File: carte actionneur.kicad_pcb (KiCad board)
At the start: 2 copper layers, 47 parts, among them J1 Conn_01x03_Pin, J10 Conn_01x03_Pin, J11 Conn_01x02, J12 Screw_Terminal_01x02, J13 Screw_Terminal_01x02, J14 Screw_Terminal_01x02, J15 Conn_01x02, J2 Conn_01x02, J3 Conn_01x03_Pin, J4 Conn_01x03_Pin, J5 Connecteur Programmation, J6 Conn_01x03_Pin, J7 Conn_01x03_Pin, J8 Conn_01x03_Pin, J9 Conn_01x03_Pin, Q1 BSS83P, Q2 2N7000, U1 MEGA_PRO_EMBED_CH340G___ATMEG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, U2 LM317_TO-252, U3 ZXBM5210-SP, U4 YAAJ_DCDC_StepDown_LM2596, U5 YAAJ_DCDC_StepDown_LM2596, U6 YAAJ_DCDC_StepDown_LM2596, U7 ZXBM5210-SP

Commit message: test git
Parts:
- added J16: Screw_Terminal_01x02, TerminalBlockBend:CUI_TBP01R1-508-02BE, F.Cu at (77.0, 130.6)
- added J17: Screw_Terminal_01x04, TerminalBlockBend:CUI_TBP01R1-508-04BE, F.Cu at (95.8, 120.4)
- added J18: Conn_01x04_Pin, Connector:FanPinHeader_1x04_P2.54mm_Vertical, F.Cu at (94.0, 127.8)
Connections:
- A1 pad 3: unconnected-(A1-1B-Pad3) -> Net-(A1-1B)
- A1 pad 4: unconnected-(A1-1A-Pad4) -> Net-(A1-1A)
- A1 pad 5: unconnected-(A1-2A-Pad5) -> Net-(A1-2A)
- A1 pad 6: unconnected-(A1-2B-Pad6) -> Net-(A1-2B)

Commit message: shema complet
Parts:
- removed C1: 0.1uF, Capacitor_SMD:C_0805_2012Metric
- removed C2: 1uF, Capacitor_SMD:C_0805_2012Metric
- removed H5, H6, H7, H8: MountingHole_Pad, MountingHole:MountingHole_2.7mm_Pad_Via
- removed J12, J13, J14, J16: Screw_Terminal_01x02, TerminalBlockBend:CUI_TBP01R1-508-02BE
- removed J18: Conn_01x04_Pin, Connector:FanPinHeader_1x04_P2.54mm_Vertical
- removed J4: Conn_01x03_Pin, Connector_PinHeader_2.54mm:PinHeader_1x03_P2.54mm_Vertical
- removed R2: 4.7k, Resistor_SMD:R_0805_2012Metric
- removed R3: 1.5k, Resistor_SMD:R_0805_2012Metric
- removed U6: YAAJ_DCDC_StepDown_LM2596, lib-buck-converter:YAAJ_DCDC_StepDown_LM2596
- added A2: Pololu_Breakout_A4988, Module:Pololu_Breakout-16_15.2x20.3mm, F.Cu at (222.9, 94.2)
- added A3: Pololu_Breakout_A4988, Module:Pololu_Breakout-16_15.2x20.3mm, F.Cu at (239.7, 94.2)
- added C7: 100µ, Capacitor_THT:CP_Radial_D8.0mm_P3.50mm, F.Cu at (224.1, 118.8)
- added C8: 100µ, Capacitor_THT:CP_Radial_D8.0mm_P3.50mm, F.Cu at (224.1, 128.3)
- added C9: 100µ, Capacitor_THT:CP_Radial_D8.0mm_P3.50mm, F.Cu at (224.1, 137.9)
- added D3: D, Diode_SMD:D_SOD-123, F.Cu at (265.0, 133.1)
- added D4: D, Diode_SMD:D_SOD-123, F.Cu at (265.0, 136.4)
- added D5: D, Diode_SMD:D_SOD-123, F.Cu at (265.0, 139.8)
- added J19: Conn_01x04_Pin, Connector_JST:JST_XH_B4B-XH-A_1x04_P2.50mm_Vertical, F.Cu at (257.9, 95.5)
- added J21: Conn_01x08_Pin, Connector_PinHeader_2.54mm:PinHeader_1x08_P2.54mm_Vertical, F.Cu at (259.8, 116.3)
- added J22: Conn_01x02_Pin, Connector_JST:JST_XH_B2B-XH-A_1x02_P2.50mm_Vertical, F.Cu at (251.5, 117.4)
- added J23: Conn_01x02_Pin, Connector_JST:JST_XH_B2B-XH-A_1x02_P2.50mm_Vertical, F.Cu at (251.5, 125.2)
- added J24: Conn_01x02_Pin, Connector_JST:JST_XH_B2B-XH-A_1x02_P2.50mm_Vertical, F.Cu at (251.5, 133.0)
- added J25: Conn_01x03_Pin, Connector_PinHeader_2.54mm:PinHeader_1x03_P2.54mm_Vertical, F.Cu at (256.8, 102.3)
- added J26: Conn_01x03_Pin, Connector_PinHeader_2.54mm:PinHeader_1x03_P2.54mm_Vertical, F.Cu at (261.4, 102.3)
- added J27: Conn_01x03_Pin, Connector_PinHeader_2.54mm:PinHeader_1x03_P2.54mm_Vertical, F.Cu at (266.1, 102.3)
- added JP1: Jumper_2_Open, Jumper:SolderJumper-2_P1.3mm_Open_TrianglePad1.0x1.5mm, F.Cu at (232.8, 115.8)
- added JP10: Jumper_2_Open, Jumper:SolderJumper-2_P1.3mm_Open_TrianglePad1.0x1.5mm, F.Cu at (237.1, 122.9)
- added JP11: Jumper_2_Open, Jumper:SolderJumper-2_P1.3mm_Open_TrianglePad1.0x1.5mm, F.Cu at (237.1, 126.4)
- added JP12: Jumper_2_Open, Jumper:SolderJumper-2_P1.3mm_Open_TrianglePad1.0x1.5mm, F.Cu at (237.1, 130.0)
- added JP13: Jumper_2_Open, Jumper:SolderJumper-2_P1.3mm_Open_TrianglePad1.0x1.5mm, F.Cu at (237.1, 133.5)
- added JP14: Jumper_2_Open, Jumper:SolderJumper-2_P1.3mm_Open_TrianglePad1.0x1.5mm, F.Cu at (237.1, 137.1)
- added JP15: Jumper_2_Open, Jumper:SolderJumper-2_P1.3mm_Open_TrianglePad1.0x1.5mm, F.Cu at (241.5, 115.8)
- added JP16: Jumper_2_Open, Jumper:SolderJumper-2_P1.3mm_Open_TrianglePad1.0x1.5mm, F.Cu at (241.5, 119.3)
- added JP17: Jumper_2_Open, Jumper:SolderJumper-2_P1.3mm_Open_TrianglePad1.0x1.5mm, F.Cu at (241.5, 122.9)
- added JP18: Jumper_2_Open, Jumper:SolderJumper-2_P1.3mm_Open_TrianglePad1.0x1.5mm, F.Cu at (241.5, 126.4)
- added JP19: Jumper_2_Open, Jumper:SolderJumper-2_P1.3mm_Open_TrianglePad1.0x1.5mm, F.Cu at (241.5, 130.0)
- added JP2: Jumper_2_Open, Jumper:SolderJumper-2_P1.3mm_Open_TrianglePad1.0x1.5mm, F.Cu at (232.8, 119.3)
- added JP20: Jumper_2_Open, Jumper:SolderJumper-2_P1.3mm_Open_TrianglePad1.0x1.5mm, F.Cu at (241.5, 133.5)
- added JP21: Jumper_2_Open, Jumper:SolderJumper-2_P1.3mm_Open_TrianglePad1.0x1.5mm, F.Cu at (241.5, 137.1)
- added JP22: Jumper_2_Open, Jumper:SolderJumper-2_P1.3mm_Open_TrianglePad1.0x1.5mm, F.Cu at (245.8, 115.8)
- added JP23: Jumper_2_Open, Jumper:SolderJumper-2_P1.3mm_Open_TrianglePad1.0x1.5mm, F.Cu at (245.8, 119.3)
- added JP24: Jumper_2_Open, Jumper:SolderJumper-2_P1.3mm_Open_TrianglePad1.0x1.5mm, F.Cu at (245.8, 122.9)
- added JP3: Jumper_2_Open, Jumper:SolderJumper-2_P1.3mm_Open_TrianglePad1.0x1.5mm, F.Cu at (232.8, 122.9)
- added JP4: Jumper_2_Open, Jumper:SolderJumper-2_P1.3mm_Open_TrianglePad1.0x1.5mm, F.Cu at (232.8, 126.4)
- added JP5: Jumper_2_Open, Jumper:SolderJumper-2_P1.3mm_Open_TrianglePad1.0x1.5mm, F.Cu at (232.8, 130.0)
- added JP6: Jumper_2_Open, Jumper:SolderJumper-2_P1.3mm_Open_TrianglePad1.0x1.5mm, F.Cu at (232.8, 133.5)
- added JP7: Jumper_2_Open, Jumper:SolderJumper-2_P1.3mm_Open_TrianglePad1.0x1.5mm, F.Cu at (232.8, 137.1)
- added JP8: Jumper_2_Open, Jumper:SolderJumper-2_P1.3mm_Open_TrianglePad1.0x1.5mm, F.Cu at (237.1, 115.8)
- added JP9: Jumper_2_Open, Jumper:SolderJumper-2_P1.3mm_Open_TrianglePad1.0x1.5mm, F.Cu at (237.1, 119.3)
- added Q3: QM6006D, Package_TO_SOT_SMD:TO-252-2, F.Cu at (166.3, 147.2)
- added Q4: QM6006D, Package_TO_SOT_SMD:TO-252-2, F.Cu at (168.5, 133.0)
- added R10: 100k, Resistor_SMD:R_0805_2012Metric, F.Cu at (270.1, 135.8)
- added R11: 100k, Resistor_SMD:R_0805_2012Metric, F.Cu at (270.1, 138.8)
- added R9: 100k, Resistor_SMD:R_0805_2012Metric, F.Cu at (270.1, 132.8)
- J17: value Screw_Terminal_01x04 -> Conn_01x04_Pin; footprint TerminalBlockBend:CUI_TBP01R1-508-04BE -> Connector_JST:JST_XH_B4B-XH-A_1x04_P2.50mm_Vertical
- J2: footprint TerminalBlock:TerminalBlock_bornier-2_P5.08mm -> TerminalBlockBend:CUI_TBP01R1-508-02BE
- J3: value Conn_01x03_Pin -> Conn_01x04_Pin; footprint Connector_PinHeader_2.54mm:PinHeader_1x03_P2.54mm_Vertical -> Connector_JST:JST_XH_B4B-XH-A_1x04_P2.50mm_Vertical
- J6: value Conn_01x03_Pin -> Conn_01x08_Pin; footprint Connector_PinHeader_2.54mm:PinHeader_1x03_P2.54mm_Vertical -> Connector_PinHeader_2.54mm:PinHeader_1x08_P2.54mm_Vertical
- Q1: value BSS83P -> Q_NMOS_GDS; footprint Package_TO_SOT_SMD:SOT-23 -> Package_TO_SOT_SMD:TO-252-2
- Q2: value 2N7000 -> QM6006D; footprint Package_TO_SOT_THT:TO-92_Inline -> Package_TO_SOT_SMD:TO-252-2
- R1: value 10k -> 56k; footprint Resistor_SMD:R_0805_2012Metric -> Resistor_SMD:R_0805_2012Metric_Pad1.20x1.40mm_HandSolder
- U2: value LM317_TO-252 -> YAAJ_DCDC_StepDown_LM2596; footprint Package_TO_SOT_SMD:TO-252-2 -> lib-buck-converter:YAAJ_DCDC_StepDown_LM2596
- moved Q2 99.4 mm to (169.8, 118.7)
- moved U2 50.0 mm to (189.2, 17.1)
- moved J2 11.2 mm to (152.2, 31.5)
- moved J3 9.07 mm to (190.2, 63.5)
- moved Q1 8.89 mm to (175.8, 47.5)
- moved J6 3.61 mm to (205.0, 64.7)
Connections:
- A1 pad 1: unconnected-(A1-GND-Pad1) -> GND
- A1 pad 10: unconnected-(A1-MS1-Pad10) -> Net-(A1-MS1)
- A1 pad 11: unconnected-(A1-MS2-Pad11) -> Net-(A1-MS2)
- A1 pad 12: unconnected-(A1-MS3-Pad12) -> Net-(A1-MS3)
- A1 pad 13: unconnected-(A1-~{RESET}-Pad13) -> Reset
- A1 pad 14: unconnected-(A1-~{SLEEP}-Pad14) -> Sleep
- A1 pad 15: unconnected-(A1-STEP-Pad15) -> STEP1
- A1 pad 16: unconnected-(A1-DIR-Pad16) -> DIR1
- A1 pad 2: unconnected-(A1-VDD-Pad2) -> +5V
- A1 pad 7: unconnected-(A1-GND-Pad7) -> GND
- A1 pad 8: unconnected-(A1-VMOT-Pad8) -> 12V Mot
- A1 pad 9: unconnected-(A1-~{ENABLE}-Pad9) -> Enable3
- C3 pad 1: tension alim moteur DC -> +5V
- C4 pad 1: +12V -> Net-(JP19-A)
- C5 pad 1: tension alim moteur DC -> +5V
- C6 pad 1: +12V -> Net-(JP22-A)
- D1 pad 1: +12V -> Net-(D1-K)
- D1 pad 2: Net-(D1-A) -> GND
- J1 pad 1: GND -> Servo4
- J1 pad 2: 5V -> 5VServo
- J1 pad 3: Net-(J1-Pin_3) -> GND
- J10 pad 1: Net-(J10-Pin_1) -> Servo3
- J10 pad 2: 5V -> 5VServo
- J17 pad 1: Net-(A1-1B) -> Net-(A2-2B)
- J17 pad 2: Net-(A1-1A) -> Net-(A2-2A)
- J17 pad 3: Net-(A1-2A) -> Net-(A2-1A)
- J17 pad 4: Net-(A1-2B) -> Net-(A2-1B)
- J2 pad 1: GND -> Net-(J2-Pin_1)
- J2 pad 2: Net-(J2-Pin_2) -> +24V
- J3 pad 1: GND -> Net-(A3-2B)
- J3 pad 2: 5V -> Net-(A3-2A)
- J3 pad 3: Net-(J3-Pin_3) -> Net-(A3-1A)
- J6 pad 1: GND -> Net-(J6-Pin_1)
- J6 pad 2: 5V -> Net-(J6-Pin_2)
- J7 pad 1: Net-(J7-Pin_1) -> Servo1
- J7 pad 2: 5V -> 5VServo
- J8 pad 1: Net-(J8-Pin_1) -> Servo2
- J8 pad 2: 5V -> 5VServo
- J9 pad 1: Net-(J9-Pin_1) -> Servo8
- J9 pad 2: 5V -> 5VServo
- Q1 pad 1: Net-(D1-A) -> Net-(D1-K)
- Q1 pad 2: +12V -> Net-(J2-Pin_1)
- Q1 pad 3: Net-(J2-Pin_2) -> GND
- Q2 pad 1: unconnected-(Q2-S-Pad1) -> ctrlActionneur1
- Q2 pad 2: unconnected-(Q2-G-Pad2) -> Net-(D3-A)
- Q2 pad 3: unconnected-(Q2-D-Pad3) -> GND
- R1 pad 1: Net-(D1-A) -> +24V
- R1 pad 2: GND -> Net-(D1-K)
- U1 pad A0: unconnected-(U1-PadA0) -> Net-(J21-Pin_8)
- U1 pad A1: unconnected-(U1-PadA1) -> Net-(J6-Pin_1)
- U1 pad A10: unconnected-(U1-PadA10) -> Net-(J21-Pin_3)
- U1 pad A11: unconnected-(U1-PadA11) -> Net-(J6-Pin_6)
- U1 pad A12: unconnected-(U1-PadA12) -> Net-(J21-Pin_2)
- U1 pad A13: unconnected-(U1-PadA13) -> Net-(J6-Pin_7)
- U1 pad A14: unconnected-(U1-PadA14) -> Net-(J21-Pin_1)
- U1 pad A15: unconnected-(U1-PadA15) -> Net-(J6-Pin_8)
- U1 pad A2: unconnected-(U1-PadA2) -> Net-(J21-Pin_7)
- U1 pad A3: unconnected-(U1-PadA3) -> Net-(J6-Pin_2)
- U1 pad A4: unconnected-(U1-PadA4) -> Net-(J21-Pin_6)
- U1 pad A5: unconnected-(U1-PadA5) -> Net-(J6-Pin_3)
- U1 pad A6: unconnected-(U1-PadA6) -> Net-(J21-Pin_5)
- U1 pad A7: unconnected-(U1-PadA7) -> Net-(J6-Pin_4)
- U1 pad A8: unconnected-(U1-PadA8) -> Net-(J21-Pin_4)
- U1 pad A9: unconnected-(U1-PadA9) -> Net-(J6-Pin_5)
- U1 pad D10: FWD1 -> Servo6
- U1 pad D11: REV1 -> Servo5
- U1 pad D12: FWD2 -> Servo8
- U1 pad D13: REV2 -> Servo7
- U1 pad D2: Net-(J7-Pin_1) -> STEP2
- U1 pad D20: unconnected-(U1-PadD20) -> SWDIO
- U1 pad D21: unconnected-(U1-PadD21) -> SWCLK
- U1 pad D22: unconnected-(U1-PadD22) -> Sleep
- U1 pad D23: unconnected-(U1-PadD23) -> Reset
- U1 pad D24: unconnected-(U1-PadD24) -> Enable3
- U1 pad D25: unconnected-(U1-PadD25) -> DIR1
- U1 pad D26: unconnected-(U1-PadD26) -> Enable2
- U1 pad D27: unconnected-(U1-PadD27) -> DIR2
- U1 pad D28: unconnected-(U1-PadD28) -> Enable1
- U1 pad D29: unconnected-(U1-PadD29) -> DIR3
- U1 pad D3: Net-(J1-Pin_3) -> STEP1
- U1 pad D4: Net-(J8-Pin_1) -> ctrlActionneur1
- U1 pad D42: unconnected-(U1-PadD42) -> ctrlActionneur2
- U1 pad D43: unconnected-(U1-PadD43) -> ctrlActionneur3
- U1 pad D44: unconnected-(U1-PadD44) -> REV2
- U1 pad D45: unconnected-(U1-PadD45) -> REV1
- U1 pad D46: unconnected-(U1-PadD46) -> FWD1
- U1 pad D5: Net-(J3-Pin_3) -> STEP3
- U1 pad D52: unconnected-(U1-PadD52) -> FWD2
- U1 pad D6: Net-(J9-Pin_1) -> Servo2
- U1 pad D7: Net-(J4-Pin_3) -> Servo1
- U1 pad D8: Net-(J10-Pin_1) -> Servo4
- U1 pad D9: Net-(J6-Pin_3) -> Servo3
- U1 pad VIN_1: +12V -> 12V Mot
- U1 pad VIN_2: +12V -> 12V Mot
- U2 pad 1: Net-(U2-ADJ) -> +24V
- U2 pad 2: +5V -> GND
- U2 pad 3: +12V -> GND
- U3 pad 2: +12V -> Net-(JP19-A)
- U3 pad 3: tension alim moteur DC -> +5V
- U3 pad 6: tension alim moteur DC -> +5V
- U4 pad 1: Net-(J12-Pin_1) -> +24V
- U4 pad 4: tension alim moteur DC -> VmotDC
- U5 pad 1: Net-(J13-Pin_1) -> +24V
- U5 pad 4: 5V -> 12V Mot
- U7 pad 2: +12V -> Net-(JP22-A)
- U7 pad 3: tension alim moteur DC -> +5V
- U7 pad 6: tension alim moteur DC -> +5V

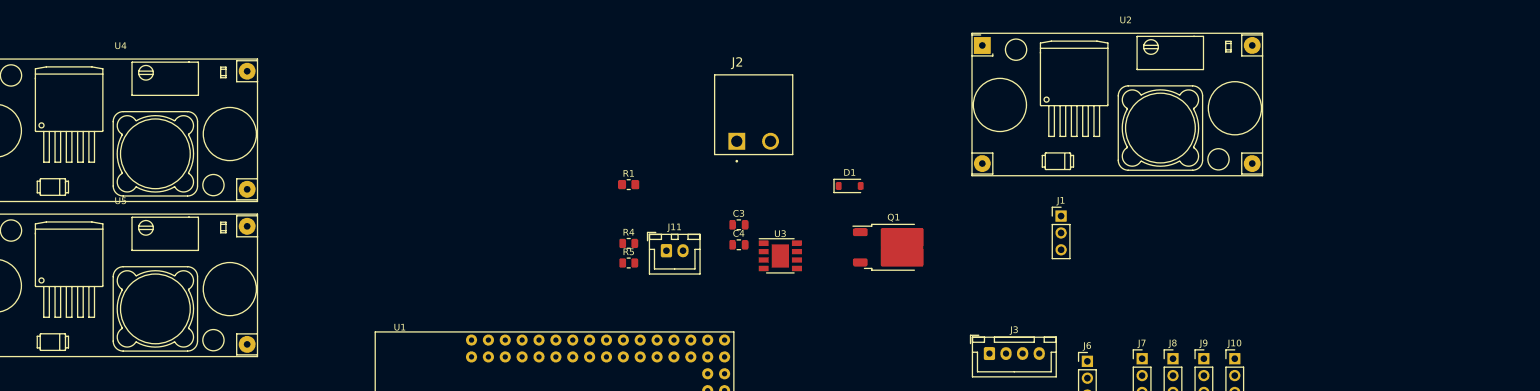
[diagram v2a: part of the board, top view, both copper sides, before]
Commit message: ajout prise capteur
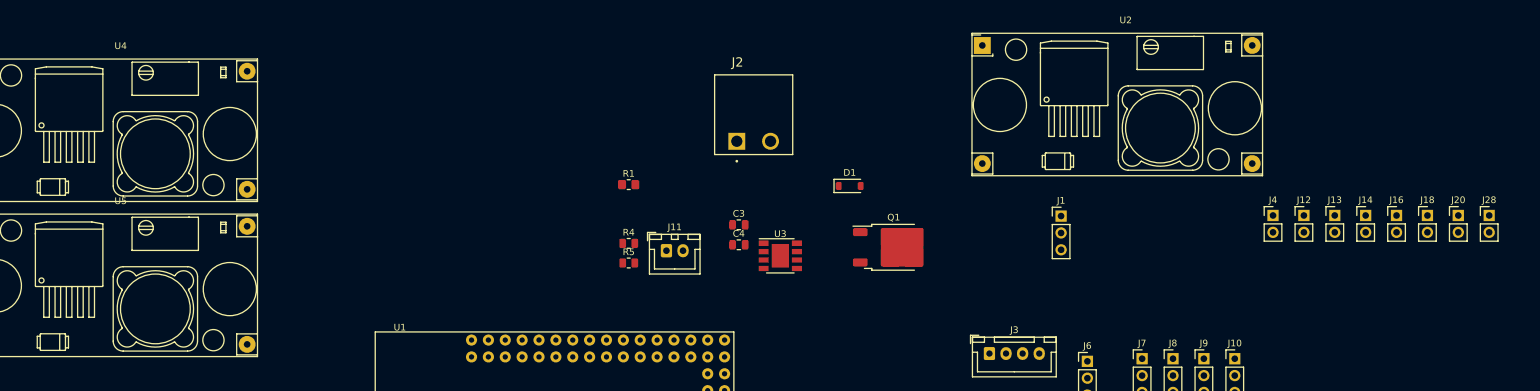
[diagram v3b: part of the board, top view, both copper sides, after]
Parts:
- added J12: Conn_01x02_Pin, Connector_PinHeader_2.54mm:PinHeader_1x02_P2.54mm_Vertical, F.Cu at (237.6, 42.7)
- added J13: Conn_01x02_Pin, Connector_PinHeader_2.54mm:PinHeader_1x02_P2.54mm_Vertical, F.Cu at (242.2, 42.7)
- added J14: Conn_01x02_Pin, Connector_PinHeader_2.54mm:PinHeader_1x02_P2.54mm_Vertical, F.Cu at (246.9, 42.7)
- added J16: Conn_01x02_Pin, Connector_PinHeader_2.54mm:PinHeader_1x02_P2.54mm_Vertical, F.Cu at (251.6, 42.7)
- added J18: Conn_01x02_Pin, Connector_PinHeader_2.54mm:PinHeader_1x02_P2.54mm_Vertical, F.Cu at (256.2, 42.7)
- added J20: Conn_01x02_Pin, Connector_PinHeader_2.54mm:PinHeader_1x02_P2.54mm_Vertical, F.Cu at (260.9, 42.7)
- added J28: Conn_01x02_Pin, Connector_PinHeader_2.54mm:PinHeader_1x02_P2.54mm_Vertical, F.Cu at (265.5, 42.7)
- added J4: Conn_01x02_Pin, Connector_PinHeader_2.54mm:PinHeader_1x02_P2.54mm_Vertical, F.Cu at (232.9, 42.7)
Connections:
- U1 pad D32: unconnected-(U1-PadD32) -> Capt1
- U1 pad D33: unconnected-(U1-PadD33) -> Capt2
- U1 pad D34: unconnected-(U1-PadD34) -> Capt3
- U1 pad D35: unconnected-(U1-PadD35) -> Capt4
- U1 pad D36: unconnected-(U1-PadD36) -> Capt5
- U1 pad D37: unconnected-(U1-PadD37) -> Capt6
- U1 pad D38: unconnected-(U1-PadD38) -> Capt7
- U1 pad D39: unconnected-(U1-PadD39) -> Capt8

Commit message: test
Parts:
- C3, C4, C5, C6, D1, D3, D4, JP1, JP13, JP14, JP15, JP16, JP17, JP18, JP19, JP2, JP20, JP21, JP22, JP23, JP24, JP3, JP4, JP5, JP6, JP7, JP8, JP9, Q1, Q2, Q3, R1, R10, R4, R5, R6, R7, R9, U1, U3, U7: moved to B.Cu
- moved J28 194.1 mm to (115.7, 166.1), turned to 90 degrees
- moved J20 184.9 mm to (116.0, 157.7), turned to 90 degrees
- moved J18 176.3 mm to (122.8, 157.9), turned to 90 degrees
- moved J16 175.2 mm to (123.3, 162.1), turned to 90 degrees
- moved D3 170.7 mm to (112.4, 56.5), turned to 90 degrees
- moved J12 170.6 mm to (115.8, 162.1), turned to 90 degrees
- moved D4 168.7 mm to (111.6, 66.3), turned to 90 degrees
- moved D5 167.3 mm to (111.0, 74.5), turned to 90 degrees
- moved J4 166.0 mm to (122.0, 166.2), turned to 90 degrees
- moved U4 165.9 mm to (186.1, 95.3), turned to 90 degrees
- moved J14 164.0 mm to (130.3, 158.1), turned to 90 degrees
- moved J13 163.9 mm to (130.0, 162.1), turned to 90 degrees
- moved R9 162.4 mm to (128.8, 52.8), turned to -90 degrees
- moved R10 159.0 mm to (128.0, 64.5), turned to -90 degrees
- moved J22 156.9 mm to (107.2, 55.6), turned to -90 degrees
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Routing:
- net GND: track 0.00 -> 1254.7 mm
- net 12V Mot: track 0.00 -> 650.8 mm, vias 0 -> 2
- net VmotDC: track 0.00 -> 356.8 mm, vias 0 -> 2
- net +5V: track 0.00 -> 289.5 mm, vias 0 -> 2
- net 5V Servo: track 0.00 -> 264.6 mm, vias 0 -> 4
- net +24V: track 0.00 -> 238.8 mm
- net ctrlActionneur1: track 0.00 -> 233.0 mm
- net ctrlActionneur3: track 0.00 -> 229.6 mm
- net ctrlActionneur2: track 0.00 -> 173.3 mm, vias 0 -> 1
- net Capt8: track 0.00 -> 125.9 mm
- net REV1: track 0.00 -> 107.5 mm
- net Capt1: track 0.00 -> 105.4 mm
- net FWD1: track 0.00 -> 101.0 mm, vias 0 -> 1
- net Reset: track 0.00 -> 94.2 mm
- net Sleep: track 0.00 -> 84.9 mm
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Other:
- board outline added: 106 x 136.7 mm

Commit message: PCB fini
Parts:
- moved C9 57.7 mm to (139.6, 117.5), turned to 90 degrees
- moved C8 57.1 mm to (139.6, 124.1), turned to -90 degrees
- moved C7 55.3 mm to (142.0, 108.1), turned to 90 degrees
- moved D1 9.74 mm to (110.5, 160.5)
- moved Q1 9.74 mm to (107.6, 155.5)
- moved J2 7.40 mm to (111.2, 149.1), turned to 90 degrees
- moved R1 6.94 mm to (115.0, 148.2), turned to -90 degrees
- moved H3 4.56 mm to (111.0, 167.0)
- moved H4 4.53 mm to (199.0, 167.0)
- moved J4 1.50 mm to (123.5, 166.2)
- moved J28 1.20 mm to (116.9, 166.1)
- moved J8 1.10 mm to (114.1, 172.6)
- moved H2 1.08 mm to (199.0, 49.0)
- moved H1 0.43 mm to (111.0, 49.0)
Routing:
- net GND: track 1254.7 -> 791.3 mm, vias 0 -> 2
- net 12V Mot: track 650.8 -> 812.7 mm, vias 2 -> 9
- net +24V: track 238.8 -> 141.5 mm
- net FWD1: track 101.0 -> 72.3 mm, vias 1 -> 0
- net Net-(J2-Pin_1): track 14.8 -> 18.2 mm
- net Net-(A3-MS3): track 66.2 -> 62.9 mm
- net Net-(A3-2B): track 23.8 -> 26.5 mm
- net Net-(A3-1A): track 28.1 -> 30.0 mm
- net Net-(A3-2A): track 27.4 -> 29.3 mm
- net Net-(A1-MS3): track 45.5 -> 47.4 mm
- net Net-(A3-1B): track 30.5 -> 32.3 mm
- net Net-(D1-K): track 12.0 -> 13.8 mm
- net 5VServo: track 71.9 -> 73.6 mm
- net Capt8: track 125.9 -> 124.2 mm
- net Capt1: track 105.4 -> 103.9 mm
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- added copper zone on B.Cu, net GND
- added copper zone on F.Cu, net GND
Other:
- board size 106 x 136.7 mm -> 108 x 138 mm
